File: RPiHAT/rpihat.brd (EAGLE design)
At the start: 65 x 56.5 mm, 37 parts

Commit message: Licensing
added License for the EEPROM design and CC4.0 BY-SA for Netz39 to the board.
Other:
- board text added: "CC 4.0 BY-SA Netz39"
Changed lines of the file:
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@@
 <circle x="3.5" y="3.5" radius="3.15" width="0" layer="41"/>
 <text x="6.985" y="49.2125" size="0.6096" layer="25" font="vector" ratio="10">1</text>
+<text x="0.3175" y="47.3075" size="0.6096" layer="25" font="vector" ratio="10" rot="R270">CC 4.0 BY-SA Netz39</text>
 </plain>
 <attributes>

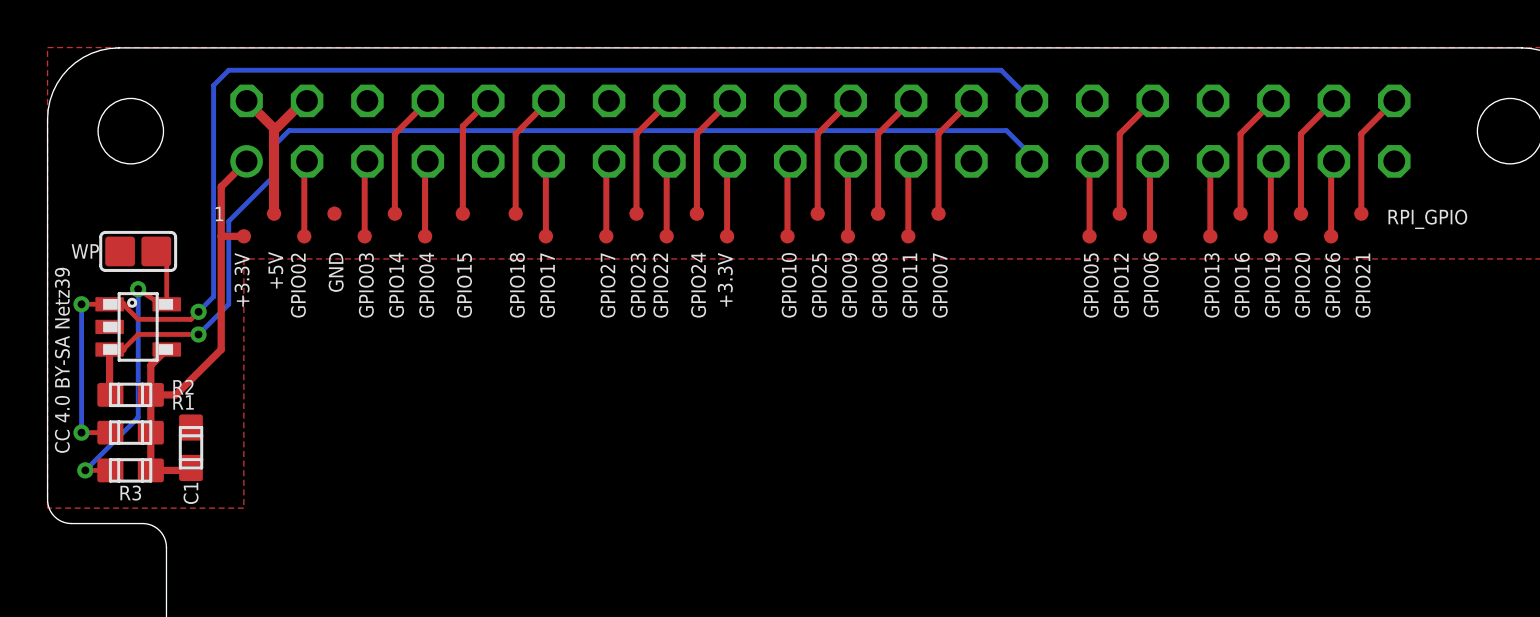
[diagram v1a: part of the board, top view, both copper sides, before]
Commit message: RPi HAT: changed all wires to 10 mil minimum
3.3V wire also changed to 10 mil, as there will be a max current of 50 mA.
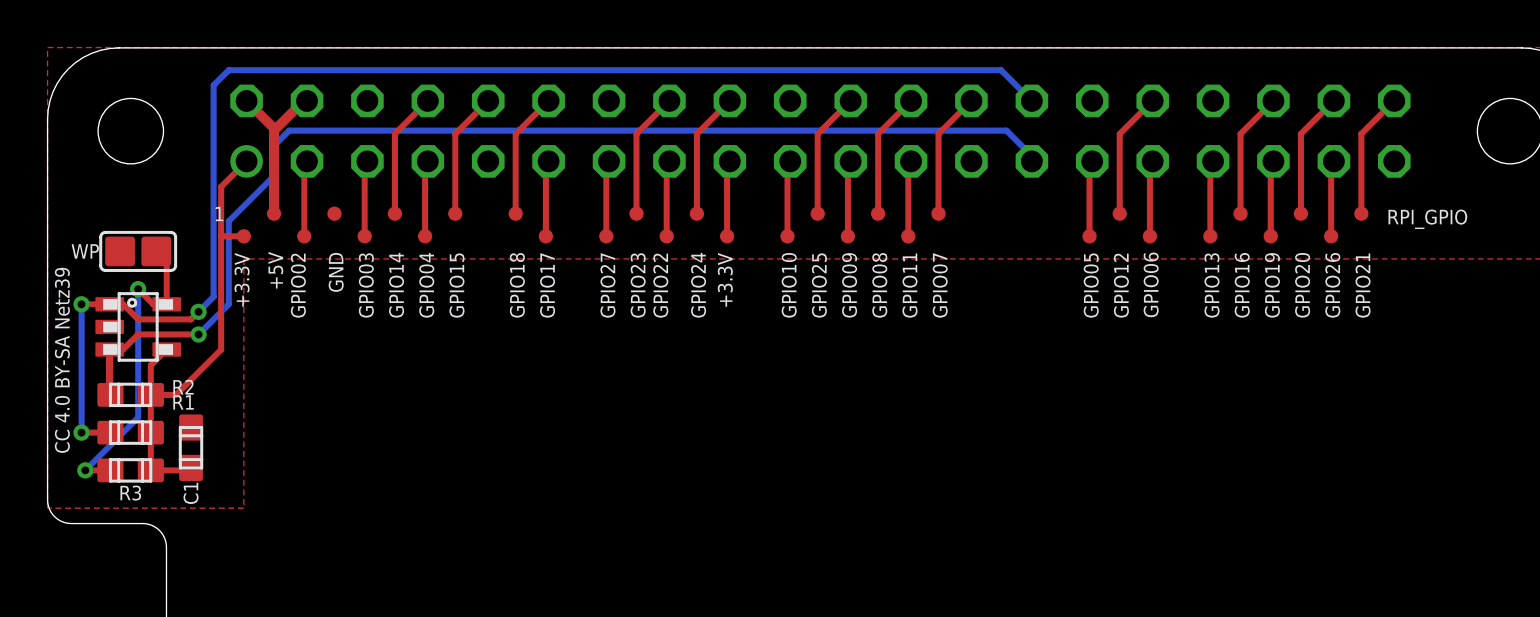
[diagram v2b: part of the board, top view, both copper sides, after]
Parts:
- moved GPIO15 0.32 mm to (17.1, 49.5)
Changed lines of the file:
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@@
 <attribute name="NAME" x="19.4501" y="47.925" size="0.6096" layer="25" font="vector" ratio="10" rot="R270"/>
 </element>
-<element name="GPIO15" library="testpad" package="TP06R" value="PTR1TP06R" x="17.4625" y="49.53" smashed="yes">
-<attribute name="TP_SIGNAL_NAME" value="" x="17.4625" y="47.625" size="1" layer="37"/>
-<attribute name="NAME" x="17.2276" y="47.925" size="0.6096" layer="25" font="vector" ratio="10" rot="R270"/>
+<element name="GPIO15" library="testpad" package="TP06R" value="PTR1TP06R" x="17.145" y="49.53" smashed="yes">
+<attribute name="TP_SIGNAL_NAME" value="" x="17.145" y="47.625" size="1" layer="37"/>
+<attribute name="NAME" x="16.9101" y="47.925" size="0.6096" layer="25" font="vector" ratio="10" rot="R270"/>
 </element>
 <element name="GPIO14" library="testpad" package="TP06R" value="PTR1TP06R" x="14.605" y="49.53" smashed="yes">
@@
 <contactref element="RPI_GPIO" pad="1"/>
 <contactref element="RPI_GPIO" pad="17"/>
-<wire x1="4.3425" y1="38.735" x2="6.0325" y2="38.735" width="0.3048" layer="1"/>
+<wire x1="4.3425" y1="38.735" x2="6.0325" y2="38.735" width="0.254" layer="1"/>
 <wire x1="6.0325" y1="38.735" x2="6.0325" y2="38.8375" width="0.3048" layer="1"/>
-<wire x1="4.3425" y1="38.735" x2="4.3425" y2="40.3225" width="0.3048" layer="1"/>
-<wire x1="4.3425" y1="40.3225" x2="4.3425" y2="41.91" width="0.3048" layer="1"/>
-<wire x1="4.3425" y1="41.91" x2="4.3425" y2="43.15" width="0.3048" layer="1"/>
-<wire x1="4.3425" y1="43.15" x2="5.01" y2="43.8175" width="0.3048" layer="1"/>
-<wire x1="8.37" y1="51.73" x2="7.3025" y2="50.6625" width="0.3048" layer="1"/>
-<wire x1="7.3025" y1="50.6625" x2="7.3025" y2="48.5775" width="0.3048" layer="1"/>
-<wire x1="7.3025" y1="48.5775" x2="7.3025" y2="43.815" width="0.3048" layer="1"/>
-<wire x1="7.3025" y1="43.815" x2="5.3975" y2="41.91" width="0.3048" layer="1"/>
-<wire x1="5.3975" y1="41.91" x2="4.3425" y2="41.91" width="0.3048" layer="1"/>
+<wire x1="4.3425" y1="38.735" x2="4.3425" y2="40.3225" width="0.254" layer="1"/>
+<wire x1="4.3425" y1="40.3225" x2="4.3425" y2="41.91" width="0.254" layer="1"/>
+<wire x1="4.3425" y1="41.91" x2="4.3425" y2="43.15" width="0.254" layer="1"/>
+<wire x1="4.3425" y1="43.15" x2="5.01" y2="43.8175" width="0.254" layer="1"/>
+<wire x1="8.37" y1="51.73" x2="7.3025" y2="50.6625" width="0.254" layer="1"/>
+<wire x1="7.3025" y1="50.6625" x2="7.3025" y2="48.5775" width="0.254" layer="1"/>
+<wire x1="7.3025" y1="48.5775" x2="7.3025" y2="43.815" width="0.254" layer="1"/>
+<wire x1="7.3025" y1="43.815" x2="5.3975" y2="41.91" width="0.254" layer="1"/>
+<wire x1="5.3975" y1="41.91" x2="4.3425" y2="41.91" width="0.254" layer="1"/>
 <contactref element="3V3" pad="TP"/>
 <contactref element="3V3_A" pad="TP"/>
-<wire x1="8.255" y1="48.5775" x2="7.3025" y2="48.5775" width="0.3048" layer="1"/>
+<wire x1="8.255" y1="48.5775" x2="7.3025" y2="48.5775" width="0.254" layer="1"/>
 <wire x1="28.575" y1="48.5775" x2="28.575" y2="51.615" width="0.254" layer="1"/>
 <wire x1="28.575" y1="51.615" x2="28.69" y2="51.73" width="0.254" layer="1"/>
@@
 <wire x1="2.61" y1="43.8175" x2="2.61" y2="42.26" width="0.3048" layer="1"/>
 <wire x1="2.61" y1="42.26" x2="2.6425" y2="41.91" width="0.3048" layer="1"/>
-<wire x1="2.61" y1="43.8175" x2="3.1775" y2="43.8175" width="0.3048" layer="1"/>
-<wire x1="3.1775" y1="43.8175" x2="3.81" y2="44.45" width="0.2032" layer="1"/>
-<wire x1="3.81" y1="44.45" x2="6.35" y2="44.45" width="0.2032" layer="1"/>
+<wire x1="2.61" y1="43.8175" x2="3.1775" y2="43.8175" width="0.254" layer="1"/>
+<wire x1="3.1775" y1="43.8175" x2="3.81" y2="44.45" width="0.254" layer="1"/>
+<wire x1="3.81" y1="44.45" x2="6.35" y2="44.45" width="0.254" layer="1"/>
 <via x="6.35" y="44.45" extent="1-16" drill="0.3302"/>
-<wire x1="6.35" y1="44.45" x2="7.62" y2="45.72" width="0.2032" layer="16"/>
-<wire x1="7.62" y1="45.72" x2="7.62" y2="49.2125" width="0.2032" layer="16"/>
-<wire x1="7.62" y1="49.2125" x2="9.525" y2="51.1175" width="0.2032" layer="16"/>
-<wire x1="9.525" y1="51.1175" x2="9.525" y2="52.3875" width="0.2032" layer="16"/>
-<wire x1="9.525" y1="52.3875" x2="10.16" y2="53.0225" width="0.2032" layer="16"/>
-<wire x1="10.16" y1="53.0225" x2="40.3225" y2="53.0225" width="0.2032" layer="16"/>
-<wire x1="40.3225" y1="53.0225" x2="41.39" y2="51.955" width="0.2032" layer="16"/>
-<wire x1="41.39" y1="51.955" x2="41.39" y2="51.73" width="0.2032" layer="16"/>
+<wire x1="6.35" y1="44.45" x2="7.62" y2="45.72" width="0.254" layer="16"/>
+<wire x1="7.62" y1="45.72" x2="7.62" y2="49.2125" width="0.254" layer="16"/>
+<wire x1="7.62" y1="49.2125" x2="9.525" y2="51.1175" width="0.254" layer="16"/>
+<wire x1="9.525" y1="51.1175" x2="9.525" y2="52.3875" width="0.254" layer="16"/>
+<wire x1="9.525" y1="52.3875" x2="10.16" y2="53.0225" width="0.254" layer="16"/>
+<wire x1="10.16" y1="53.0225" x2="40.3225" y2="53.0225" width="0.254" layer="16"/>
+<wire x1="40.3225" y1="53.0225" x2="41.39" y2="51.955" width="0.254" layer="16"/>
+<wire x1="41.39" y1="51.955" x2="41.39" y2="51.73" width="0.254" layer="16"/>
 </signal>
 <signal name="ID_SC">
@@
 <contactref element="IC" pad="1"/>
 <contactref element="RPI_GPIO" pad="28"/>
-<wire x1="2.61" y1="45.7175" x2="3.1775" y2="45.7175" width="0.3048" layer="1"/>
-<wire x1="3.1775" y1="45.7175" x2="3.81" y2="45.085" width="0.2032" layer="1"/>
-<wire x1="3.81" y1="45.085" x2="6.0325" y2="45.085" width="0.2032" layer="1"/>
-<wire x1="6.0325" y1="45.085" x2="6.35" y2="45.4025" width="0.2032" layer="1"/>
-<wire x1="2.6425" y1="40.3225" x2="1.42875" y2="40.3225" width="0.2032" layer="1"/>
+<wire x1="2.61" y1="45.7175" x2="3.1775" y2="45.7175" width="0.254" layer="1"/>
+<wire x1="3.1775" y1="45.7175" x2="3.81" y2="45.085" width="0.254" layer="1"/>
+<wire x1="3.81" y1="45.085" x2="6.0325" y2="45.085" width="0.254" layer="1"/>
+<wire x1="6.0325" y1="45.085" x2="6.35" y2="45.4025" width="0.254" layer="1"/>
+<wire x1="2.6425" y1="40.3225" x2="1.42875" y2="40.3225" width="0.254" layer="1"/>
 <via x="1.42875" y="40.3225" extent="1-16" drill="0.3302"/>
-<wire x1="1.42875" y1="40.3225" x2="1.42875" y2="45.72" width="0.2032" layer="16"/>
+<wire x1="1.42875" y1="40.3225" x2="1.42875" y2="45.72" width="0.254" layer="16"/>
 <via x="1.42875" y="45.72" extent="1-16" drill="0.3302"/>
-<wire x1="1.42875" y1="45.72" x2="2.6075" y2="45.72" width="0.2032" layer="1"/>
+<wire x1="1.42875" y1="45.72" x2="2.6075" y2="45.72" width="0.254" layer="1"/>
 <wire x1="2.6075" y1="45.72" x2="2.61" y2="45.7175" width="0.3048" layer="1"/>
 <via x="6.35" y="45.4025" extent="1-16" drill="0.3302"/>
-<wire x1="6.35" y1="45.4025" x2="6.985" y2="46.0375" width="0.2032" layer="16"/>
-<wire x1="6.985" y1="46.0375" x2="6.985" y2="54.9275" width="0.2032" layer="16"/>
-<wire x1="6.985" y1="54.9275" x2="7.62" y2="55.5625" width="0.2032" layer="16"/>
-<wire x1="7.62" y1="55.5625" x2="40.0975" y2="55.5625" width="0.2032" layer="16"/>
-<wire x1="40.0975" y1="55.5625" x2="41.39" y2="54.27" width="0.2032" layer="16"/>
+<wire x1="6.35" y1="45.4025" x2="6.985" y2="46.0375" width="0.254" layer="16"/>
+<wire x1="6.985" y1="46.0375" x2="6.985" y2="54.9275" width="0.254" layer="16"/>
+<wire x1="6.985" y1="54.9275" x2="7.62" y2="55.5625" width="0.254" layer="16"/>
+<wire x1="7.62" y1="55.5625" x2="40.0975" y2="55.5625" width="0.254" layer="16"/>
+<wire x1="40.0975" y1="55.5625" x2="41.39" y2="54.27" width="0.254" layer="16"/>
 </signal>
 <signal name="WP">
@@
 <contactref element="R3" pad="1"/>
 <contactref element="IC" pad="5"/>
-<wire x1="5.01" y1="45.7175" x2="5.01" y2="47.5025" width="0.2032" layer="1"/>
+<wire x1="5.01" y1="45.7175" x2="5.01" y2="47.5025" width="0.254" layer="1"/>
 <wire x1="5.01" y1="47.5025" x2="4.57" y2="47.9425" width="0.3048" layer="1"/>
 <wire x1="5.01" y1="45.7175" x2="4.765" y2="45.7175" width="0.3048" layer="1"/>
-<wire x1="4.765" y1="45.7175" x2="3.81" y2="46.355" width="0.2032" layer="1"/>
 <via x="3.81" y="46.355" extent="1-16" drill="0.3302"/>
-<wire x1="3.81" y1="46.355" x2="3.81" y2="40.9575" width="0.2032" layer="16"/>
-<wire x1="3.81" y1="40.9575" x2="1.5875" y2="38.735" width="0.2032" layer="16"/>
+<wire x1="3.81" y1="46.355" x2="3.81" y2="40.9575" width="0.254" layer="16"/>
+<wire x1="3.81" y1="40.9575" x2="1.5875" y2="38.735" width="0.254" layer="16"/>
 <via x="1.5875" y="38.735" extent="1-16" drill="0.3302"/>
-<wire x1="1.5875" y1="38.735" x2="2.6425" y2="38.735" width="0.2032" layer="1"/>
+<wire x1="1.5875" y1="38.735" x2="2.6425" y2="38.735" width="0.254" layer="1"/>
+<wire x1="3.81" y1="46.355" x2="4.4475" y2="45.7175" width="0.254" layer="1"/>
+<wire x1="4.4475" y1="45.7175" x2="5.01" y2="45.7175" width="0.254" layer="1"/>
 </signal>
 <signal name="RPI_GPIO21">
 <contactref element="RPI_GPIO" pad="40"/>
 <contactref element="GPIO21" pad="TP"/>
-<wire x1="55.245" y1="49.53" x2="55.245" y2="52.885" width="0.254" layer="1"/>
-<wire x1="55.245" y1="52.885" x2="56.63" y2="54.27" width="0.254" layer="1"/>
+<wire x1="56.63" y1="54.27" x2="55.245" y2="52.885" width="0.254" layer="1"/>
+<wire x1="55.245" y1="52.885" x2="55.245" y2="49.53" width="0.254" layer="1"/>
 </signal>
 <signal name="RPI_GPIO20">
@@
 <contactref element="RPI_GPIO" pad="10"/>
 <contactref element="GPIO15" pad="TP"/>
-<wire x1="17.4625" y1="49.53" x2="17.4625" y2="53.2025" width="0.254" layer="1"/>
-<wire x1="17.4625" y1="53.2025" x2="18.53" y2="54.27" width="0.254" layer="1"/>
+<wire x1="17.145" y1="49.53" x2="17.145" y2="52.885" width="0.254" layer="1"/>
+<wire x1="17.145" y1="52.885" x2="18.53" y2="54.27" width="0.254" layer="1"/>
 </signal>
 <signal name="RPI_GPIO14">

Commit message: RPi HAT: Documentation
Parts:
- moved WP 0.32 mm to (3.81, 47.6)
- renumbered IC to U1
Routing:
- net WP: track 13.7 -> 15.5 mm
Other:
- board text added: "500mA from the 5V pins,"
- board text added: "Cutout is optinonal"
- board text added: "ID EEPROM"
- board text added: "When drawing more than"
- board text added: "and may be removed."
- board text added: "re-wire accordingly!"
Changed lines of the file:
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@@
 <circle x="3.5" y="3.5" radius="3.15" width="0" layer="41"/>
 <text x="6.985" y="49.2125" size="0.6096" layer="25" font="vector" ratio="10">1</text>
-<text x="0.3175" y="47.3075" size="0.6096" layer="25" font="vector" ratio="10" rot="R270">CC 4.0 BY-SA Netz39</text>
+<text x="6.6675" y="0.635" size="0.6096" layer="25" font="vector" ratio="10">CC 4.0 BY-SA Netz39</text>
+<text x="10.16" y="42.8625" size="0.6096" layer="48">When drawing more than</text>
+<text x="10.16" y="41.91" size="0.6096" layer="48">500mA from the 5V pins,</text>
+<text x="10.16" y="40.9575" size="0.6096" layer="48">re-wire accordingly!</text>
+<wire x1="0.635" y1="48.5775" x2="6.985" y2="48.5775" width="0.1524" layer="25"/>
+<wire x1="6.985" y1="48.5775" x2="6.985" y2="37.1475" width="0.1524" layer="25"/>
+<wire x1="6.985" y1="37.1475" x2="0.635" y2="37.1475" width="0.1524" layer="25"/>
+<wire x1="0.635" y1="37.1475" x2="0.635" y2="48.5775" width="0.1524" layer="25"/>
+<text x="6.0325" y="49.53" size="0.6096" layer="25" font="vector" ratio="10" rot="R180">ID EEPROM</text>
+<wire x1="9.525" y1="44.1325" x2="20.0025" y2="44.1325" width="0.254" layer="48"/>
+<wire x1="20.0025" y1="44.1325" x2="20.0025" y2="40.005" width="0.254" layer="48"/>
+<wire x1="20.0025" y1="40.005" x2="9.525" y2="40.005" width="0.254" layer="48"/>
+<wire x1="9.525" y1="40.005" x2="9.525" y2="44.1325" width="0.254" layer="48"/>
+<text x="6.35" y="30.48" size="0.6096" layer="48">Cutout is optinonal</text>
+<text x="6.35" y="29.5275" size="0.6096" layer="48">and may be removed.</text>
+<text x="47.3075" y="18.0975" size="0.6096" layer="48">Cutout is optinonal</text>
+<text x="47.3075" y="16.8275" size="0.6096" layer="48">and may be removed.</text>
 </plain>
 <attributes>
@@
 <attribute name="VALUE" x="7.1" y="57.699" size="1.27" layer="28" ratio="10" rot="MR180"/>
 </element>
-<element name="WP" library="we-rcl" package="JUMPER2_NC" value="JUMPER2-NOCREAM" x="3.81" y="47.9425" smashed="yes" rot="R90">
-<attribute name="NAME" x="1.5875" y="47.9425" size="0.6096" layer="25" font="vector" ratio="10" rot="R180" align="center"/>
+<element name="WP" library="we-rcl" package="JUMPER2_NC" value="JUMPER2-NOCREAM" x="3.81" y="47.625" smashed="yes" rot="R90">
+<attribute name="NAME" x="1.5875" y="47.625" size="0.6096" layer="25" font="vector" ratio="10" rot="R180" align="center"/>
 </element>
 <element name="C1" library="we-rcl" package="R0603" value="100n" x="6.0325" y="39.6875" smashed="yes">
-<attribute name="NAME" x="6.0325" y="37.7825" size="0.6096" layer="25" font="vector" ratio="10" rot="R270" align="center"/>
+<attribute name="NAME" x="6.35" y="37.7825" size="0.6096" layer="25" font="vector" ratio="10" align="center"/>
 </element>
 <element name="R1" library="we-rcl" package="R0603" value="3k9" x="3.4925" y="40.3225" smashed="yes" rot="R90">
@@
 <attribute name="NAME" x="3.4925" y="37.7825" size="0.6096" layer="25" font="vector" ratio="10" align="center"/>
 </element>
-<element name="IC" library="we-chip" package="SOT23-5" value="24LC-I/OT" x="3.81" y="44.7675" smashed="yes">
+<element name="U1" library="we-chip" package="SOT23-5" value="24LC-I/OT" x="3.81" y="44.7675" smashed="yes">
 <attribute name="DIGIKEY" value="24LC32AT-I/OTDKR-ND" x="-17.78" y="46.0375" size="1.778" layer="27" display="off"/>
-<attribute name="VALUE" x="1.5875" y="43.4975" size="0.4064" layer="27" font="vector" ratio="10" rot="R270" align="center"/>
+<attribute name="NAME" x="3.81" y="44.7675" size="0.8128" layer="25" font="vector" ratio="10" rot="R270" align="center"/>
+<attribute name="VALUE" x="6.35" y="44.7675" size="0.8128" layer="27" font="vector" ratio="10" rot="R270" align="center"/>
 </element>
 <element name="GPIO06" library="testpad" package="TP06R" value="PTR1TP06R" x="46.355" y="48.5775" smashed="yes" rot="R270">
@@
 <signals>
 <signal name="GND">
-<contactref element="IC" pad="2"/>
+<contactref element="U1" pad="2"/>
 <contactref element="WP" pad="1"/>
 <contactref element="C1" pad="1"/>
@@
 <signal name="+3V3">
 <contactref element="R2" pad="2"/>
-<contactref element="IC" pad="4"/>
+<contactref element="U1" pad="4"/>
 <contactref element="R3" pad="2"/>
 <contactref element="C1" pad="2"/>
@@
 <signal name="ID_SD">
 <contactref element="R2" pad="1"/>
-<contactref element="IC" pad="3"/>
+<contactref element="U1" pad="3"/>
 <contactref element="RPI_GPIO" pad="27"/>
 <wire x1="2.61" y1="43.8175" x2="2.61" y2="42.26" width="0.3048" layer="1"/>
@@
 <signal name="ID_SC">
 <contactref element="R1" pad="1"/>
-<contactref element="IC" pad="1"/>
+<contactref element="U1" pad="1"/>
 <contactref element="RPI_GPIO" pad="28"/>
 <wire x1="2.61" y1="45.7175" x2="3.1775" y2="45.7175" width="0.254" layer="1"/>
@@
 <contactref element="WP" pad="2"/>
 <contactref element="R3" pad="1"/>
-<contactref element="IC" pad="5"/>
+<contactref element="U1" pad="5"/>
 <wire x1="5.01" y1="45.7175" x2="5.01" y2="47.5025" width="0.254" layer="1"/>
-<wire x1="5.01" y1="47.5025" x2="4.57" y2="47.9425" width="0.3048" layer="1"/>
+<wire x1="5.01" y1="47.5025" x2="4.57" y2="47.625" width="0.3048" layer="1"/>
 <wire x1="5.01" y1="45.7175" x2="4.765" y2="45.7175" width="0.3048" layer="1"/>
-<via x="3.81" y="46.355" extent="1-16" drill="0.3302"/>
-<wire x1="3.81" y1="46.355" x2="3.81" y2="40.9575" width="0.254" layer="16"/>
-<wire x1="3.81" y1="40.9575" x2="1.5875" y2="38.735" width="0.254" layer="16"/>
-<via x="1.5875" y="38.735" extent="1-16" drill="0.3302"/>
-<wire x1="1.5875" y1="38.735" x2="2.6425" y2="38.735" width="0.254" layer="1"/>
-<wire x1="3.81" y1="46.355" x2="4.4475" y2="45.7175" width="0.254" layer="1"/>
+<via x="6.35" y="46.355" extent="1-16" drill="0.3302"/>
+<wire x1="3.81" y1="41.11625" x2="1.42875" y2="38.735" width="0.254" layer="16"/>
+<via x="1.42875" y="38.735" extent="1-16" drill="0.3302"/>
+<wire x1="1.42875" y1="38.735" x2="2.6425" y2="38.735" width="0.254" layer="1"/>
 <wire x1="4.4475" y1="45.7175" x2="5.01" y2="45.7175" width="0.254" layer="1"/>
+<wire x1="6.35" y1="46.355" x2="5.7125" y2="45.7175" width="0.254" layer="1"/>
+<wire x1="5.7125" y1="45.7175" x2="5.01" y2="45.7175" width="0.254" layer="1"/>
+<wire x1="3.81" y1="41.11625" x2="3.81" y2="43.815" width="0.254" layer="16"/>
+<wire x1="3.81" y1="43.815" x2="6.35" y2="46.355" width="0.254" layer="16"/>
 </signal>
 <signal name="RPI_GPIO21">
@@
 <wire x1="53.975" y1="51.615" x2="54.09" y2="51.73" width="0.254" layer="1"/>
 </signal>
+<signal name="N$1">
+</signal>
 </signals>
